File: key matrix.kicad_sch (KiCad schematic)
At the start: 62 parts, among them J3 Conn_01x04_MountingPin, J4 Conn_01x04_MountingPin, SW1 SW_Push, SW10 SW_Push, SW11 SW_Push, SW12 SW_Push, SW13 SW_Push, SW14 SW_Push, SW15 SW_Push, SW16 SW_Push, SW17 SW_Push, SW18 SW_Push, SW19 SW_Push, SW2 SW_Push, SW20 SW_Push, SW21 SW_Push, SW22 SW_Push, SW23 SW_Push, SW24 SW_Push, SW25 SW_Push, SW26 SW_Push, SW27 SW_Push, SW28 SW_Push, SW29 SW_Push, SW3 SW_Push, SW30 SW_Push, SW31 SW_Push, SW32 SW_Push, SW33 SW_Push, SW34 SW_Push, SW35 SW_Push, SW36 SW_Push, SW37 SW_Push, SW38 SW_Push, SW39 SW_Push, SW4 SW_Push, SW40 SW_Push, SW41 SW_Push, SW42 SW_Push, SW43 RotaryEncoder_Switch_MP, SW44 RotaryEncoder_Switch_MP, SW45 SW_Push, SW46 SW_Push, SW47 SW_Push, SW48 SW_Push, SW5 SW_Push, SW6 SW_Push, SW7 SW_Push, SW8 SW_Push, SW9 SW_Push, U1 BAT54CTB6_R1_00001, U10 BAT54CTB6_R1_00001, U11 BAT54CTB6_R1_00001, U12 BAT54CTB6_R1_00001, U2 BAT54CTB6_R1_00001, U3 BAT54CTB6_R1_00001, U4 BAT54CTB6_R1_00001, U5 BAT54CTB6_R1_00001, U6 BAT54CTB6_R1_00001, U7 BAT54CTB6_R1_00001, U8 BAT54CTB6_R1_00001, U9 BAT54CTB6_R1_00001

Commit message: parpar v2 RC2
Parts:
- SW1, SW10, SW11, SW12, SW13, SW14, SW15, SW16, SW17, SW18, SW19, SW2, SW20, SW21, SW22, SW23, SW24, SW25, SW26, SW27, SW28, SW29, SW3, SW30, SW31, SW32, SW33, SW34, SW35, SW36, SW37, SW38, SW39, SW4, SW40, SW41, SW42, SW5, SW6, SW7, SW8, SW9: footprint coquette_footprints:choc1u-hs-modded -> coquette_footprints:SW_Hotswap_Kailh_Choc_V1V2_Plated_modded; symbol Switch:SW_Push -> Switch:SW_Push_Shielded
- SW45, SW46, SW47, SW48: symbol Switch:SW_Push -> Switch:SW_Push_Shielded
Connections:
- net GND: now also SW1.SH (B), SW10.SH (B), SW11.SH (B), SW12.SH (B), SW13.SH (B), SW14.SH (B), SW15.SH (B), SW16.SH (B), SW17.SH (B), SW18.SH (B), SW19.SH (B), SW2.SH (B), SW20.SH (B), SW21.SH (B), SW22.SH (B), SW23.SH (B), SW24.SH (B), SW25.SH (B), SW26.SH (B), SW27.SH (B), SW28.SH (B), SW29.SH (B), SW3.SH (B), SW30.SH (B), SW31.SH (B), SW32.SH (B), SW33.SH (B), SW34.SH (B), SW35.SH (B), SW36.SH (B), SW37.SH (B), SW38.SH (B), SW39.SH (B), SW4.SH (B), SW40.SH (B), SW41.SH (B), SW42.SH (B), SW45.SH (B), SW46.SH (B), SW47.SH (B), SW48.SH (B), SW5.SH (B), SW6.SH (B), SW7.SH (B), SW8.SH (B), SW9.SH (B)
- net c0 renamed col_a
- net c0a renamed mtx_a0
- net mtx_a0: now also SW1.2; no longer SW1.1
- net c0b renamed mtx_a1
- net mtx_a1: now also SW5.2; no longer SW5.1
- net c0c renamed mtx_a2
- net mtx_a2: now also SW11.2; no longer SW11.1
- net c0d renamed mtx_a3
- net mtx_a3: now also SW17.2; no longer SW17.1
- net c0e renamed mtx_a4
- net mtx_a4: now also SW22.2; no longer SW22.1
- net c0f renamed mtx_a5
- net mtx_a5: now also SW27.2; no longer SW27.1
- net c0g renamed mtx_a6
- net mtx_a6: now also SW33.2; no longer SW33.1
- net c0h renamed mtx_a7
- net mtx_a7: now also SW39.2; no longer SW39.1
- net c1 renamed col_b
- net c1a renamed mtx_b0
- net mtx_b0: now also SW2.2; no longer SW2.1
- net c1b renamed mtx_b1
- net mtx_b1: now also SW6.2; no longer SW6.1
- net c1c renamed mtx_b2
- net mtx_b2: now also SW12.2; no longer SW12.1
- net c1d renamed mtx_b3
- net mtx_b3: now also SW18.2; no longer SW18.1
- net c1e renamed mtx_b4
- net mtx_b4: now also SW23.2; no longer SW23.1
- net c1f renamed mtx_b5
- net mtx_b5: now also SW28.2; no longer SW28.1
- net c1g renamed mtx_b6
- net mtx_b6: now also SW34.2; no longer SW34.1
- net c1h renamed mtx_b7
- net mtx_b7: now also SW40.2; no longer SW40.1
- net c2 renamed col_c
- net c2a renamed mtx_c0
- net mtx_c0: now also J3.1 (Pin_1)
- net c2b renamed mtx_c1
- net mtx_c1: now also SW7.2; no longer SW7.1
- net c2c renamed mtx_c2
- net mtx_c2: now also SW13.2; no longer SW13.1
- net c2d renamed mtx_c3
- net c2e renamed mtx_c4
- net mtx_c4: now also SW24.2; no longer SW24.1
- net c2f renamed mtx_c5
- net mtx_c5: now also SW29.2; no longer SW29.1
- net c2g renamed mtx_c6
- net mtx_c6: now also SW35.2; no longer SW35.1
- net c2h renamed mtx_c7
- net c3 renamed col_d
- net c3a renamed mtx_d0
- net mtx_d0: no longer J3.1 (Pin_1)
- net c3b renamed mtx_d1
- net mtx_d1: now also SW8.2; no longer SW8.1
- net c3c renamed mtx_d2
- net mtx_d2: now also SW14.2; no longer SW14.1
- net c3d renamed mtx_d3
- net mtx_d3: now also SW19.2; no longer SW19.1
- net c3e renamed mtx_d4
- net c3f renamed mtx_d5
- net mtx_d5: now also SW30.2; no longer SW30.1
- net c3g renamed mtx_d6
- net mtx_d6: now also SW36.2; no longer SW36.1
- net c3h renamed mtx_d7
- net c4 renamed col_e
- net c4a renamed mtx_e0
- net mtx_e0: now also SW3.2; no longer SW3.1
- net c4b renamed mtx_e1
- net mtx_e1: now also SW9.2; no longer SW9.1
- net c4c renamed mtx_e2
- net mtx_e2: now also SW15.2; no longer SW15.1
- net c4d renamed mtx_e3
- net mtx_e3: now also SW20.2; no longer SW20.1
- net c4e renamed mtx_e4
- net mtx_e4: now also SW25.2; no longer SW25.1
- net c4f renamed mtx_e5
- net mtx_e5: now also SW31.2; no longer SW31.1
- net c4g renamed mtx_e6
- net mtx_e6: now also SW37.2; no longer SW37.1
- net c4h renamed mtx_e7
- net mtx_e7: now also SW41.2; no longer SW41.1
- net c5 renamed col_f
- net c5a renamed mtx_f0
- net mtx_f0: now also SW4.2; no longer SW4.1
- net c5b renamed mtx_f1
- net mtx_f1: now also SW10.2; no longer SW10.1
- net c5c renamed mtx_f2
- net mtx_f2: now also SW16.2; no longer SW16.1
- net c5d renamed mtx_f3
- net mtx_f3: now also SW21.2; no longer SW21.1
- net c5e renamed mtx_f4
- net mtx_f4: now also SW26.2; no longer SW26.1
- net c5f renamed mtx_f5
- net mtx_f5: now also SW32.2; no longer SW32.1
- net c5g renamed mtx_f6
- net mtx_f6: now also SW38.2; no longer SW38.1
- net c5h renamed mtx_f7
- net mtx_f7: now also SW42.2; no longer SW42.1
- removed net row_a: J3.3 (Pin_3), SW1.2, SW2.2, SW3.2, SW4.2, SW45.1, SW46.2
- removed net row_b: SW10.2, SW5.2, SW6.2, SW7.2, SW8.2, SW9.2
- removed net row_c: SW11.2, SW12.2, SW13.2, SW14.2, SW15.2, SW16.2
- removed net row_d: SW17.2, SW18.2, SW19.2, SW20.2, SW21.2, SW43.S1
- removed net row_e: SW22.2, SW23.2, SW24.2, SW25.2, SW26.2, SW44.S2
- removed net row_f: SW27.2, SW28.2, SW29.2, SW30.2, SW31.2, SW32.2
- removed net row_g: SW33.2, SW34.2, SW35.2, SW36.2, SW37.2, SW38.2
- removed net row_h: J4.3 (Pin_3), SW39.2, SW40.2, SW41.2, SW42.2, SW47.1, SW48.2
- new net row_0: J3.3 (Pin_3), SW1.1, SW2.1, SW3.1, SW4.1, SW45.1, SW46.2
- new net row_1: SW10.1, SW5.1, SW6.1, SW7.1, SW8.1, SW9.1
- new net row_2: SW11.1, SW12.1, SW13.1, SW14.1, SW15.1, SW16.1
- new net row_3: SW17.1, SW18.1, SW19.1, SW20.1, SW21.1, SW43.S1
- new net row_4: SW22.1, SW23.1, SW24.1, SW25.1, SW26.1, SW44.S2
- new net row_5: SW27.1, SW28.1, SW29.1, SW30.1, SW31.1, SW32.1
- new net row_6: SW33.1, SW34.1, SW35.1, SW36.1, SW37.1, SW38.1
- new net row_7: J4.3 (Pin_3), SW39.1, SW40.1, SW41.1, SW42.1, SW47.1, SW48.2
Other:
- moved on the sheet: J3, J4, SW43, SW44, U1, U10, U11, U12, U2, U3, U4, U5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

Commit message: parpar v2 RC3
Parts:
- added C44, C45, C46, C47: 10nF, Capacitor_SMD:C_0402_1005Metric, symbol Device:C
- added R2, R3, R4, R5: 10k, Resistor_SMD:R_0603_1608Metric, symbol Device:R_US
- SW43, SW44: footprint marbastlib-various:ROT_Alps_EC11E-Switch -> coquette_footprints:PEC12R-4215F-S0024
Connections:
- net GND: now also C44.2, C45.2, C46.2, C47.2
- net ec1a: now also C45.1, R2.2; no longer SW43.A
- net ec1b: now also C44.1, R3.2; no longer SW43.B
- net ec2a: now also C47.1, R4.2; no longer SW44.A
- net ec2b: now also C46.1, R5.2; no longer SW44.B
- net mtx_c0: no longer J3.1 (Pin_1)
- net mtx_c3: now also SW43.S1; no longer SW43.S2
- net mtx_d0: now also J3.1 (Pin_1)
- net mtx_d4: now also SW44.S2; no longer SW44.S1
- net row_3: now also SW43.S2; no longer SW43.S1
- net row_4: now also SW44.S1; no longer SW44.S2
- new net: R3.1, SW43.B
- new net: R2.1, SW43.A
- new net: R5.1, SW44.B
- new net: R4.1, SW44.A
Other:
- moved on the sheet: SW43, SW44

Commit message: parpar v2 RC6
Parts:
- C44, C45, C46, C47: footprint Capacitor_SMD:C_0402_1005Metric -> Capacitor_SMD:C_0603_1608Metric
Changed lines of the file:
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@@
 			)
 		)
-		(property "Footprint" "Capacitor_SMD:C_0402_1005Metric"
+		(property "Footprint" "Capacitor_SMD:C_0603_1608Metric"
 			(at 205.74 150.1648 0)
 			(effects
@@
 			)
 		)
-		(property "Footprint" "Capacitor_SMD:C_0402_1005Metric"
+		(property "Footprint" "Capacitor_SMD:C_0603_1608Metric"
 			(at 250.19 150.1648 0)
 			(effects
@@
 			)
 		)
-		(property "Footprint" "Capacitor_SMD:C_0402_1005Metric"
+		(property "Footprint" "Capacitor_SMD:C_0603_1608Metric"
 			(at 205.74 157.7848 0)
 			(effects
@@
 			)
 		)
-		(property "Footprint" "Capacitor_SMD:C_0402_1005Metric"
+		(property "Footprint" "Capacitor_SMD:C_0603_1608Metric"
 			(at 250.19 157.7848 0)
 			(effects

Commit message: parpar v2 RC6
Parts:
- J3, J4: value Conn_01x04_MountingPin -> JST_SUR_SM04B-SURS-TF
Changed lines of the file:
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@@
 			)
 		)
-		(property "Value" "Conn_01x04_MountingPin"
+		(property "Value" "JST_SUR_SM04B-SURS-TF"
 			(at 153.67 154.0255 0)
 			(effects
@@
 			)
 		)
-		(property "Value" "Conn_01x04_MountingPin"
+		(property "Value" "JST_SUR_SM04B-SURS-TF"
 			(at 153.67 133.7055 0)
 			(effects

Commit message: really final????
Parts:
- SW45, SW46, SW47, SW48: footprint Button_Switch_SMD:SW_SPST_B3U-3100P -> coquette_footprints:SMD4_SW_EVQP7J_PAN; symbol Switch:SW_Push_Shielded -> Switch:SW_Push
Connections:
- net GND: no longer SW45.SH (B), SW46.SH (B), SW47.SH (B), SW48.SH (B)
- net mtx_d0: now also SW46.2; no longer SW46.1
- net mtx_d7: now also SW48.2; no longer SW48.1
- net row_0: now also SW46.1; no longer SW46.2
- net row_7: now also SW48.1; no longer SW48.2

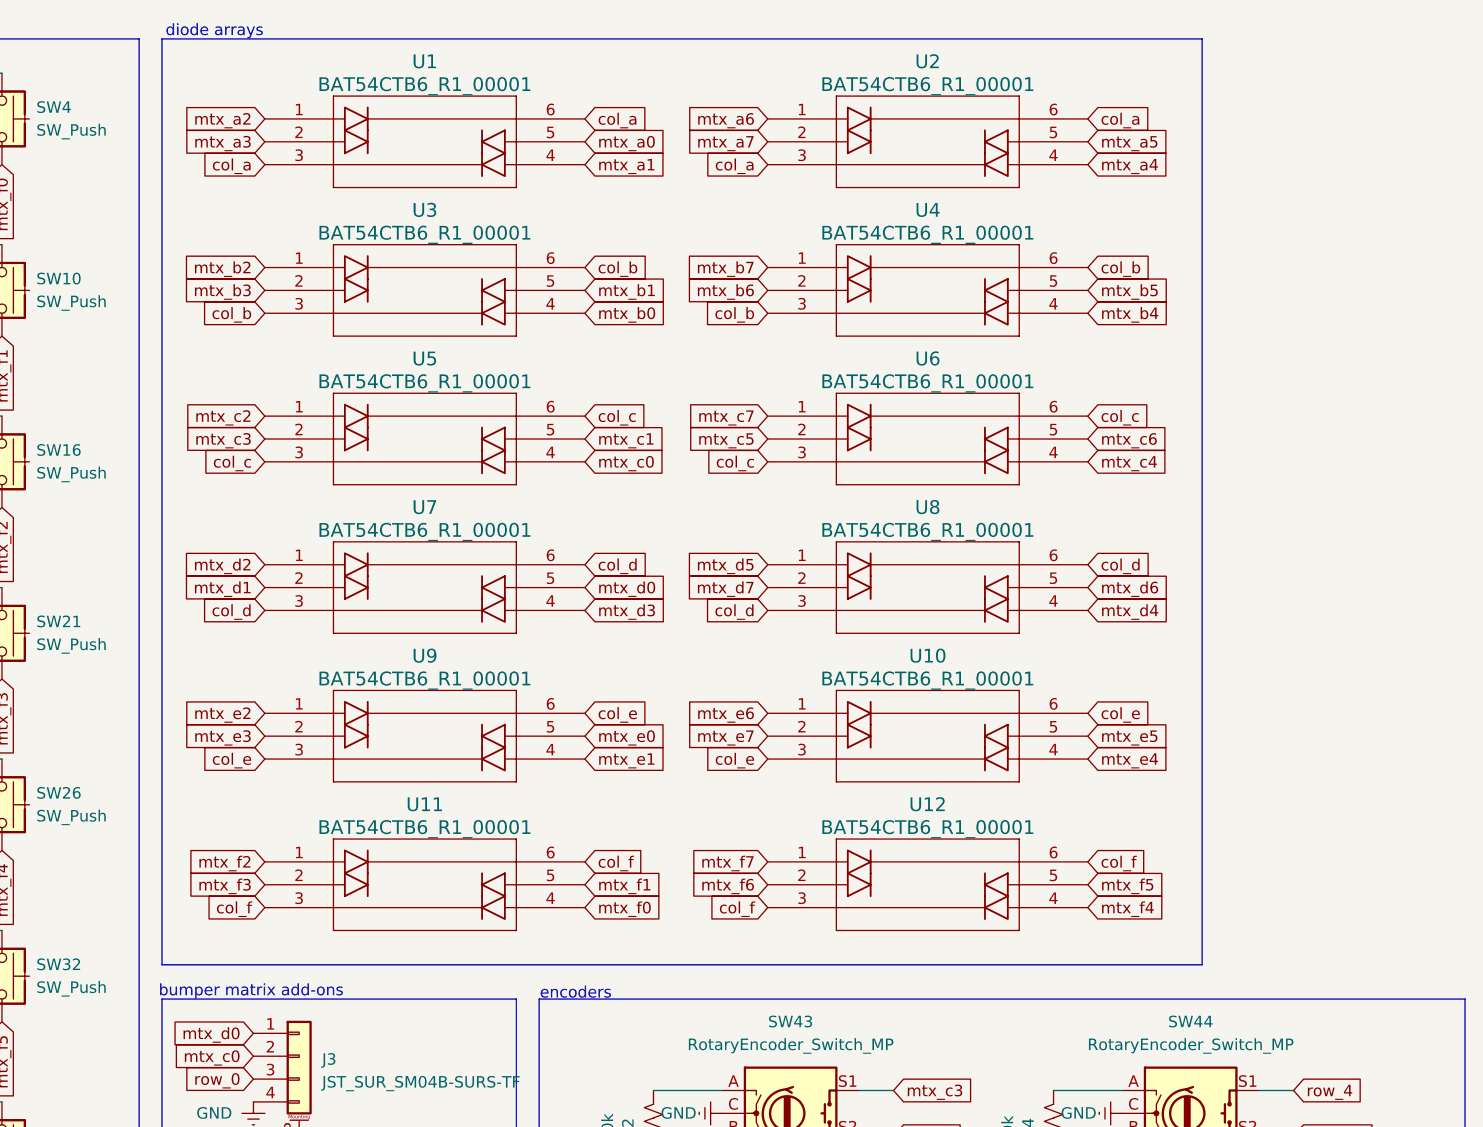
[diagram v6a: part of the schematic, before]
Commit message: column resistors to further bolster protection against esd events and shorts
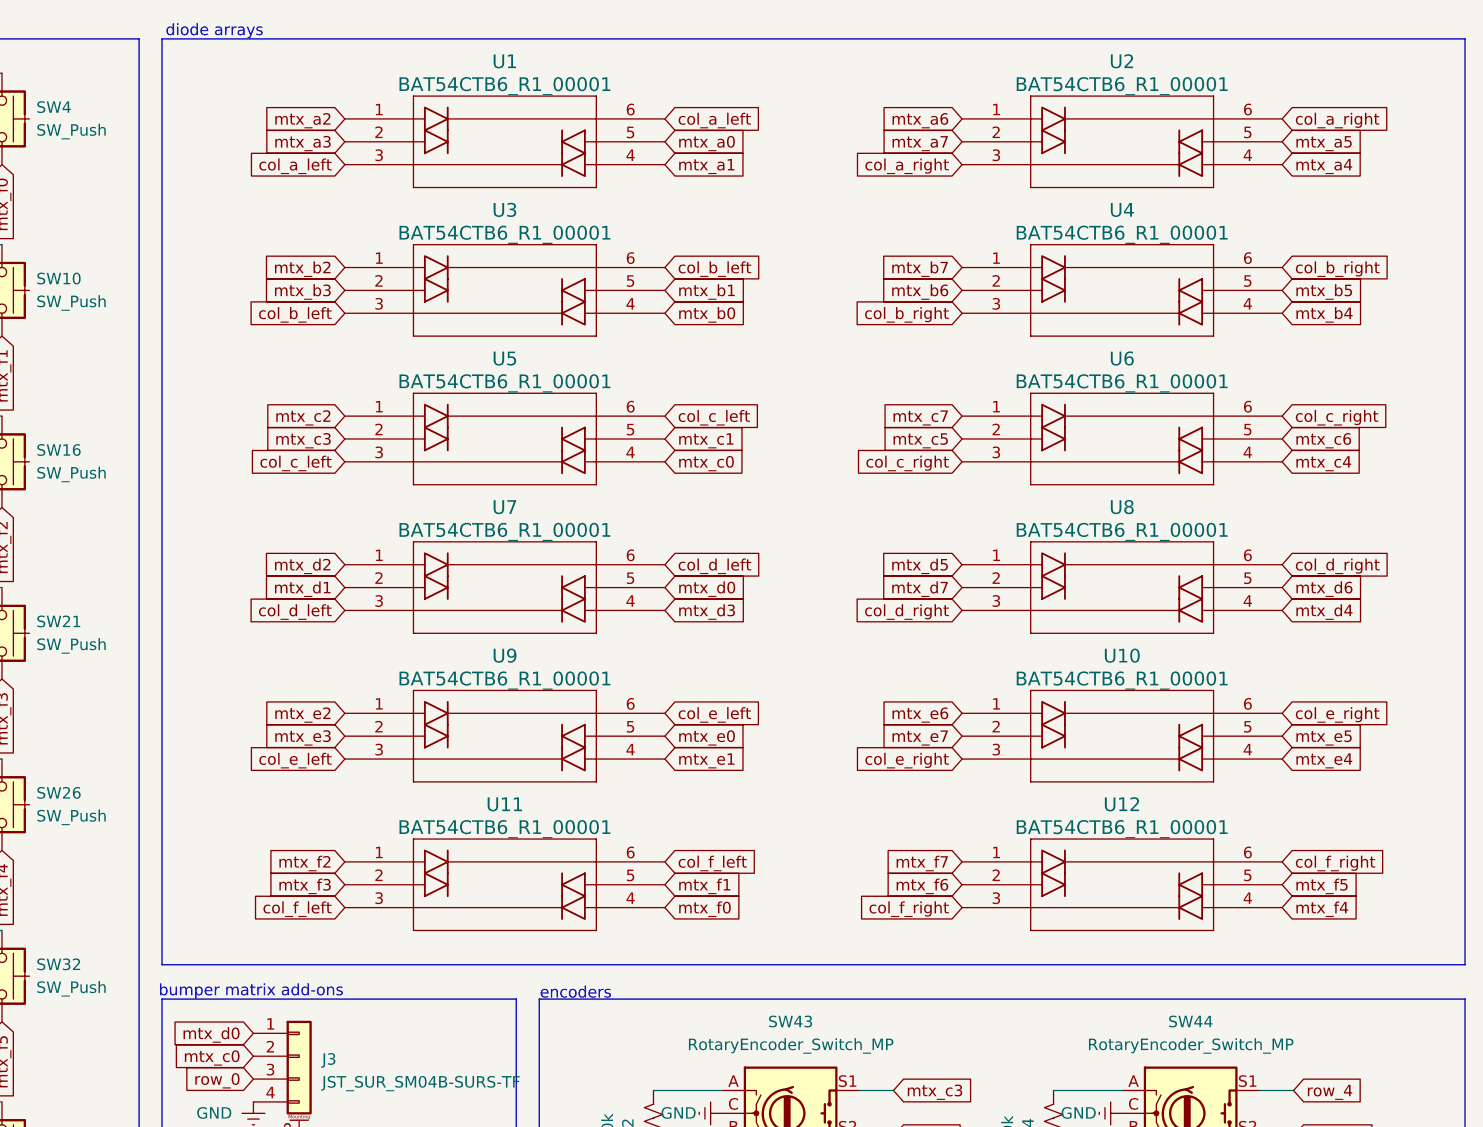
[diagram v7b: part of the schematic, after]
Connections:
- net col_a renamed col_a_left
- net col_a_left: no longer U2.3, U2.6
- net col_b renamed col_b_left
- net col_b_left: no longer U4.3, U4.6
- net col_c renamed col_c_left
- net col_c_left: no longer U6.3, U6.6
- net col_d renamed col_d_left
- net col_d_left: no longer U8.3, U8.6
- net col_e renamed col_e_left
- net col_e_left: no longer U10.3, U10.6
- net col_f renamed col_f_left
- net col_f_left: no longer U12.3, U12.6
- new net col_a_right: U2.3, U2.6
- new net col_b_right: U4.3, U4.6
- new net col_c_right: U6.3, U6.6
- new net col_d_right: U8.3, U8.6
- new net col_e_right: U10.3, U10.6
- new net col_f_right: U12.3, U12.6
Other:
- moved on the sheet: U1, U10, U11, U12, U2, U3, U4, U5, U6, U7, U8, U9

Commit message: actually production version, for real?
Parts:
- removed SW45, SW46, SW47, SW48: SW_Push, coquette_footprints:SMD4_SW_EVQP7J_PAN, symbol Switch:SW_Push
- added SW49, SW50: SW_rocker, coquette_footprints:TMHU27, symbol coquette_symbols:SW_rocker
- SW1, SW10, SW11, SW12, SW13, SW14, SW15, SW16, SW17, SW18, SW19, SW2, SW20, SW21, SW22, SW23, SW24, SW25, SW26, SW27, SW28, SW29, SW3, SW30, SW31, SW32, SW33, SW34, SW35, SW36, SW37, SW38, SW39, SW4, SW40, SW41, SW42, SW5, SW6, SW7, SW8, SW9: footprint coquette_footprints:SW_Hotswap_Kailh_Choc_V1V2_Plated_modded -> coquette_footprints:SW_Choc_V1_V2_hotswap
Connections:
- net GND: now also SW49.MP, SW50.MP
- net mtx_c0: now also SW49.2
- net mtx_c5: now also U6.1; no longer U6.2
- net mtx_c7: now also U6.2, SW50.1; no longer U6.1
- net mtx_d0: now also SW49.1
- net mtx_d7: now also SW50.2
- net row_0: now also SW49.3 (Common)
- net row_7: now also SW50.3 (Common)
